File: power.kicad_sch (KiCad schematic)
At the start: 62 parts, among them J1 USB_C_Receptacle_USB2.0_14P, Q2 Q_NMOS_GDS, SW2 SW_SPDT, U12 AT24CS08-STUM, U2 BQ25895RTW, U4 LM1117DT-3.3, U5 MCP4017-xxxxLT, U6 TPS25751DREFR_C30169739, U7 LM3478MA

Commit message: resistor values
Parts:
- F1: Comment (none) -> resetable please
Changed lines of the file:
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@@
 			)
 		)
-		(property "Comment" ""
+		(property "Comment" "resetable please"
 			(at 54.61 30.48 90)
 			(hide yes)

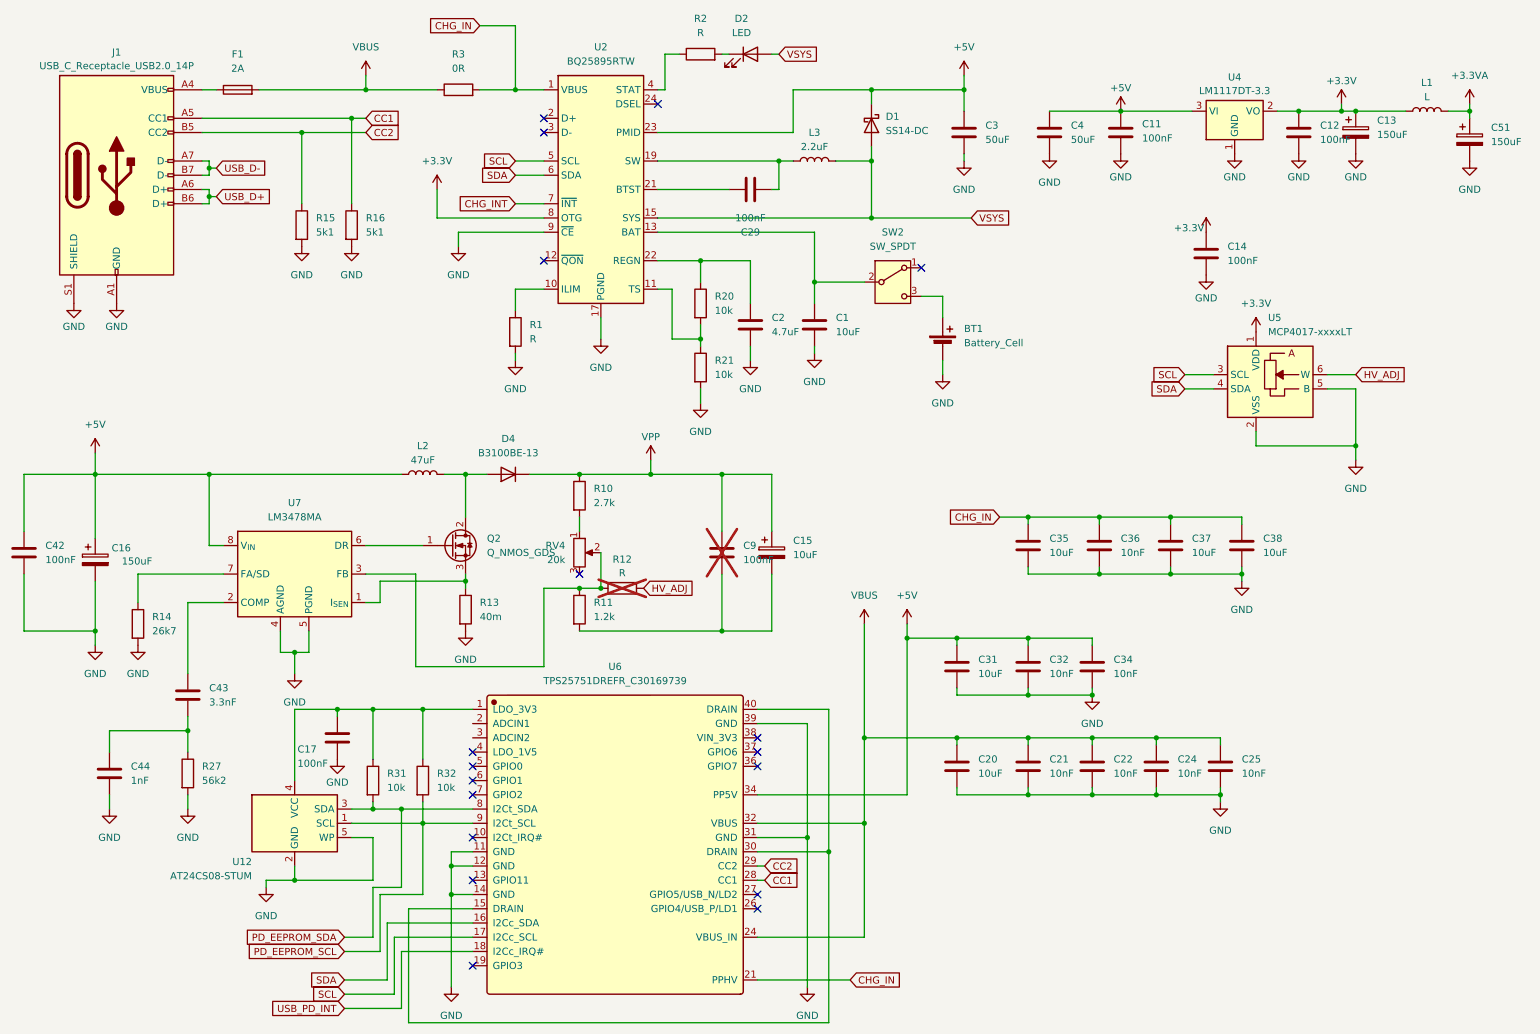
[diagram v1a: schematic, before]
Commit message: test points and small fix
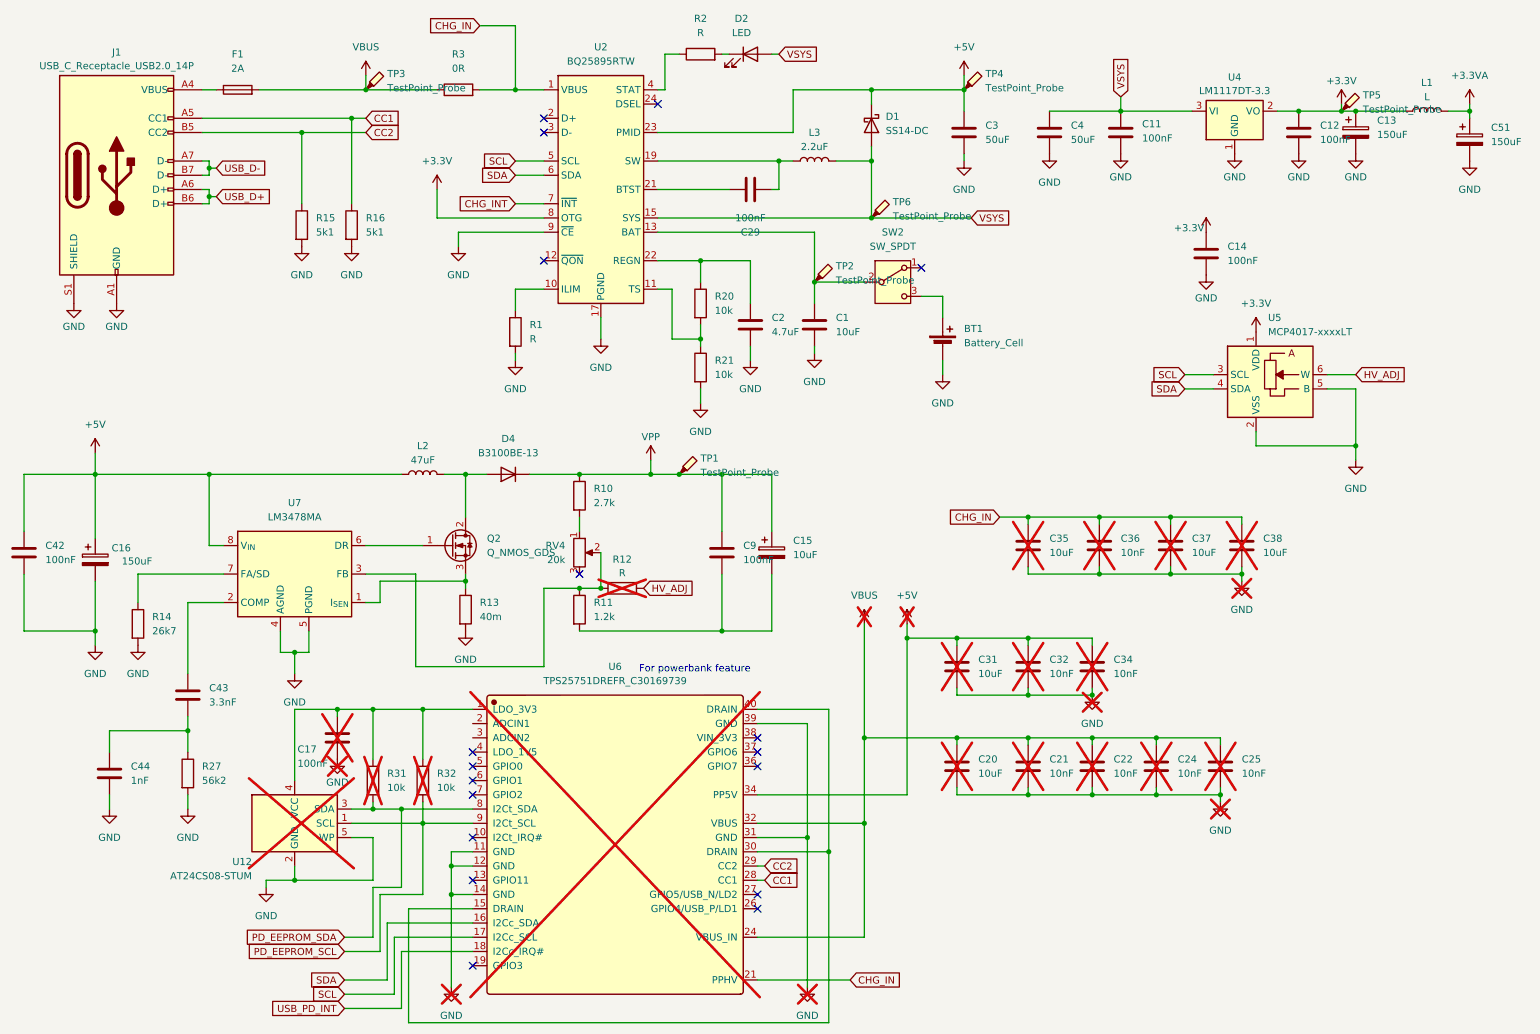
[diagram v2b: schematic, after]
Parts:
- added TP1, TP2, TP3, TP4, TP5, TP6: TestPoint_Probe, symbol Connector:TestPoint_Probe
- C17, C20, C21, C22, C24, C25, C31, C32, C34, C35, C36, C37, C38, R31, R32, U12, U6: now not fitted
- C9: now fitted
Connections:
- net +3.3V: now also TP5.1
- net +5V: now also TP4.1; no longer C11.1, C4.1, U4.3 (VI)
- net VBUS: now also TP3.1
- net VPP: now also TP1.1
- net VSYS: now also C11.1, C4.1, U4.3 (VI), TP6.1
- net at C1.1, SW2.2 (B), U2.13 (BAT)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: now also TP2.1
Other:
- note added: "For powerbank feature"

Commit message: sensor heat and some testpoints
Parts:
- TP1, TP2, TP3, TP4, TP5, TP6: footprint (none) -> TestPoint:TestPoint_THTPad_D2.0mm_Drill1.0mm
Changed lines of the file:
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@@
 			)
 		)
-		(property "Footprint" ""
+		(property "Footprint" "TestPoint:TestPoint_THTPad_D2.0mm_Drill1.0mm"
 			(at 172.72 53.34 0)
 			(hide yes)
@@
 			)
 		)
-		(property "Footprint" ""
+		(property "Footprint" "TestPoint:TestPoint_THTPad_D2.0mm_Drill1.0mm"
 			(at 82.55 30.48 0)
 			(hide yes)
@@
 			)
 		)
-		(property "Footprint" ""
+		(property "Footprint" "TestPoint:TestPoint_THTPad_D2.0mm_Drill1.0mm"
 			(at 162.56 64.77 0)
 			(hide yes)
@@
 			)
 		)
-		(property "Footprint" ""
+		(property "Footprint" "TestPoint:TestPoint_THTPad_D2.0mm_Drill1.0mm"
 			(at 189.23 30.48 0)
 			(hide yes)
@@
 			)
 		)
-		(property "Footprint" ""
+		(property "Footprint" "TestPoint:TestPoint_THTPad_D2.0mm_Drill1.0mm"
 			(at 256.54 34.29 0)
 			(hide yes)
@@
 			)
 		)
-		(property "Footprint" ""
+		(property "Footprint" "TestPoint:TestPoint_THTPad_D2.0mm_Drill1.0mm"
 			(at 138.43 99.06 0)
 			(hide yes)

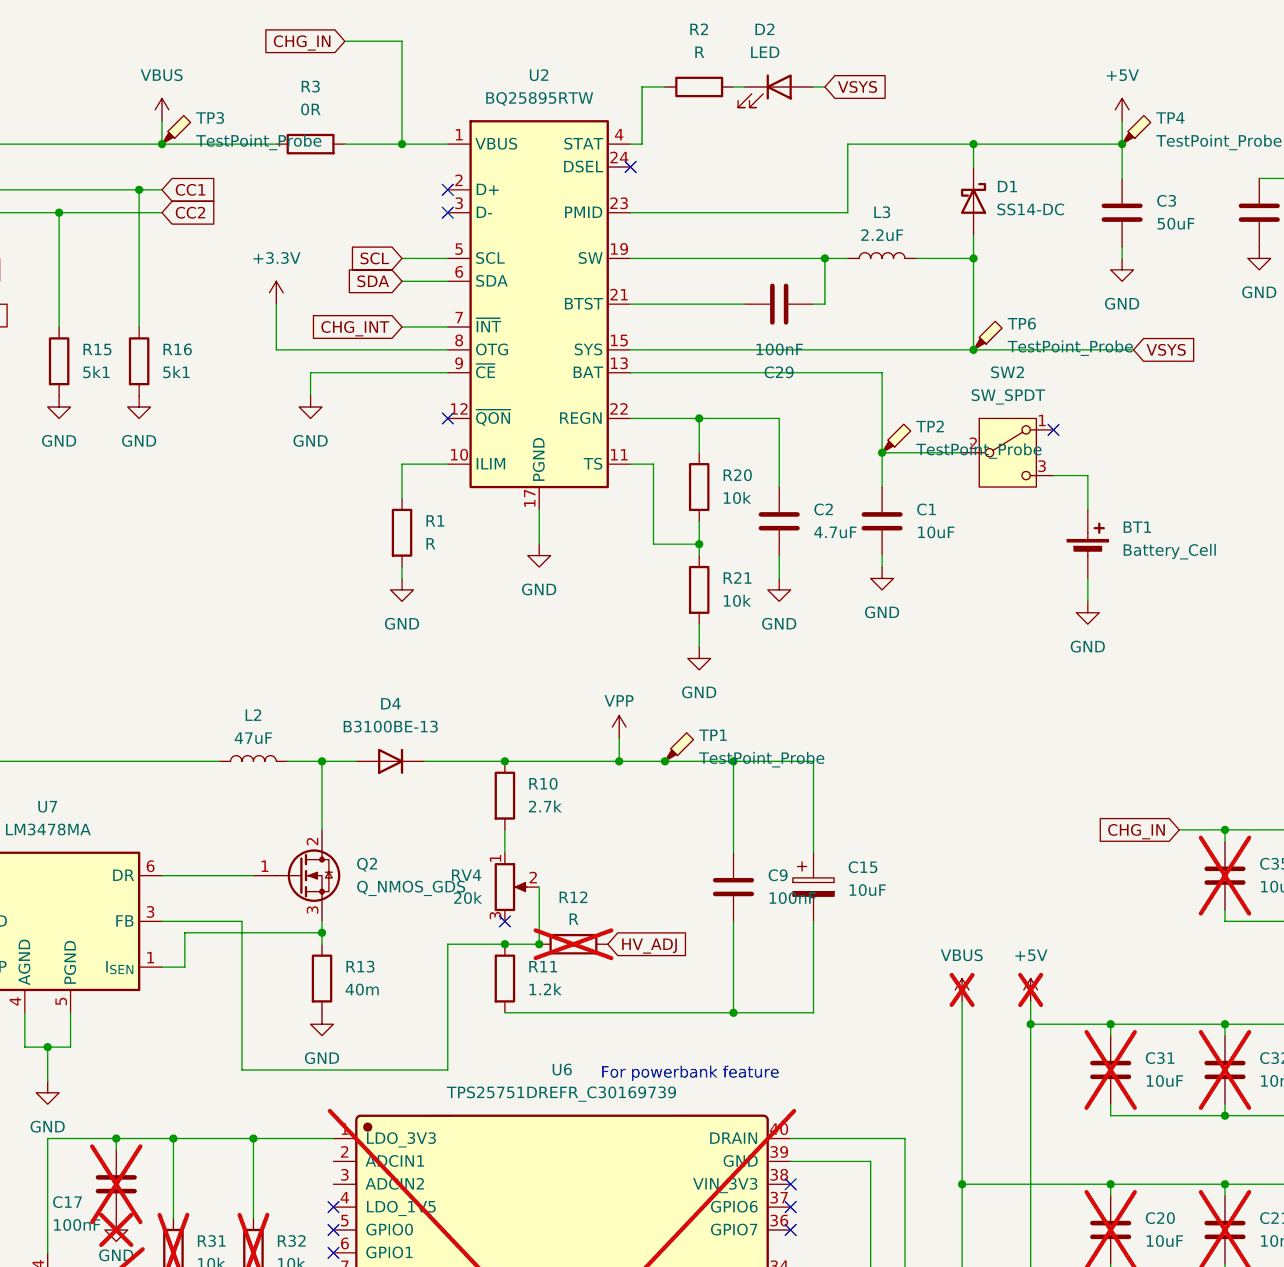
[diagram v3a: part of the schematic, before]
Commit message: some parts placement
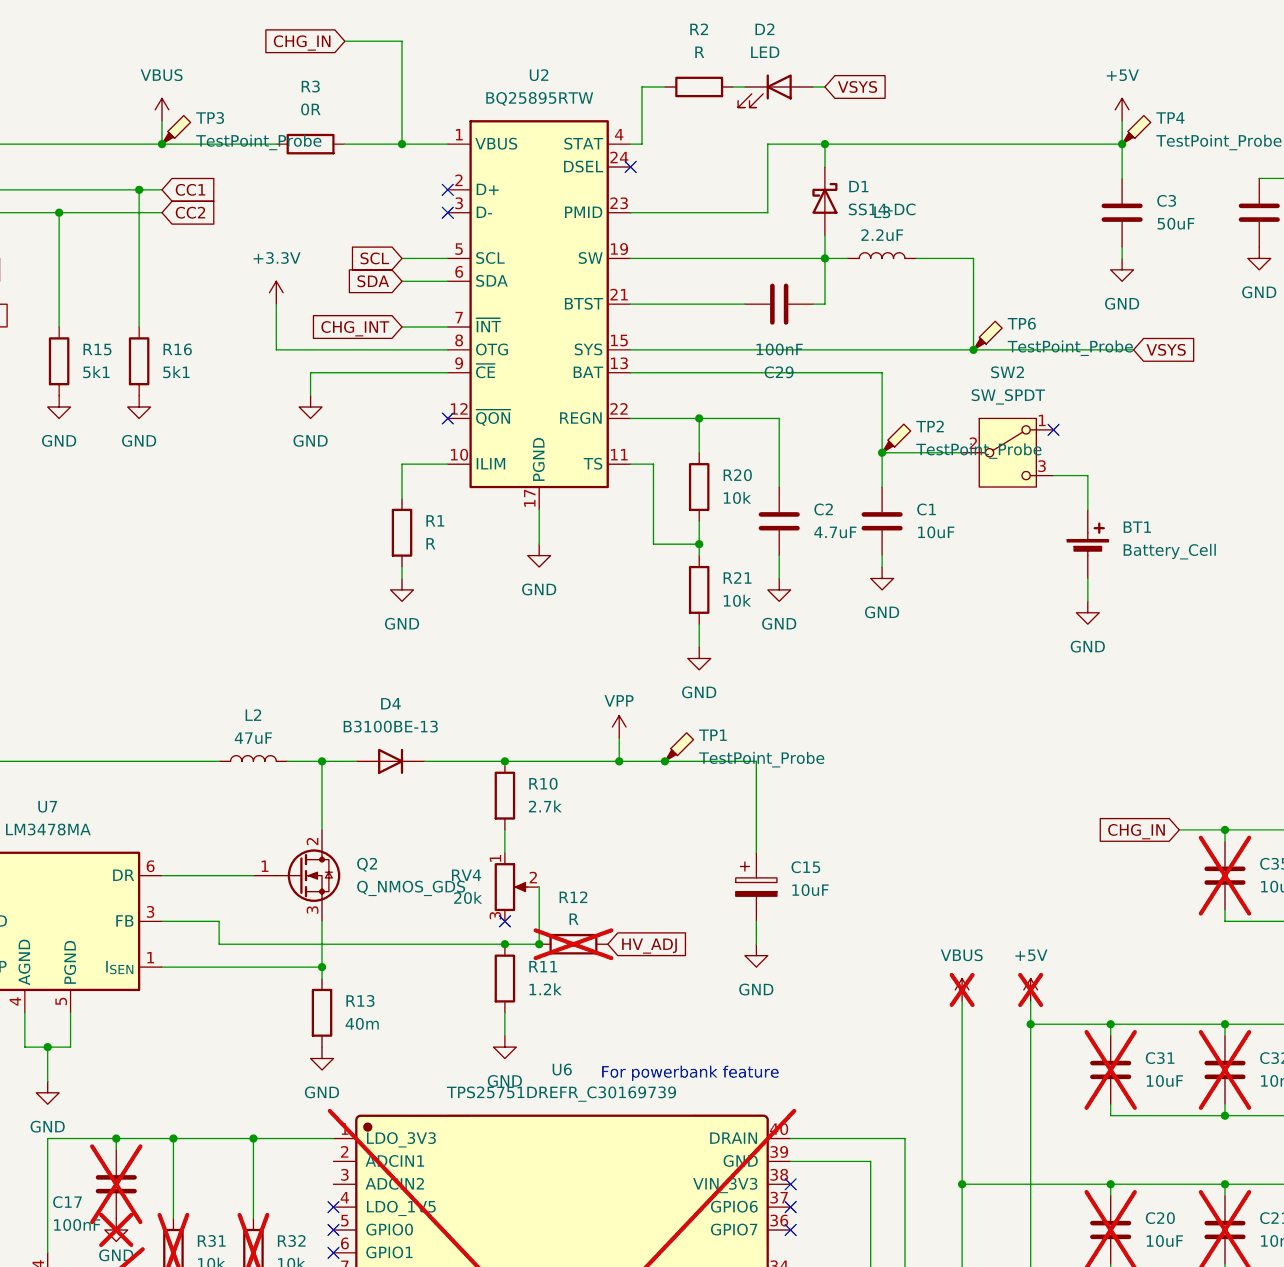
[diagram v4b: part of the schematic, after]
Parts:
- removed C9: 100nF, Capacitor_SMD:C_2220_5750Metric, symbol Device:C
- D1: footprint (none) -> Diode_SMD:D_SMA
- SW2: footprint Button_Switch_THT:SW_XKB_DM1-16UD-1 -> Button_Switch_SMD:SW_SPDT_CK_JS102011SAQN
- U12: footprint (none) -> Package_TO_SOT_SMD:SOT-23-5
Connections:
- net GND: now also C15.2, R11.2
- net VSYS: no longer D1.2 (A)
- net at C29.1, L3.1, U2.19 (SW)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: now also D1.2 (A)
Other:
- moved on the sheet: C15, R13

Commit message: Component changes, some new feature
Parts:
- removed C15: 10uF, Capacitor_SMD:CP_Elec_5x4.5, symbol Device:C_Polarized
- removed C16: 150uF, Capacitor_SMD:CP_Elec_5x4.5, symbol Device:C_Polarized
- removed C17: 100nF, Capacitor_SMD:C_0805_2012Metric, symbol Device:C
- removed C20, C31, C35, C37, C38: 10uF, Capacitor_SMD:C_0805_2012Metric, symbol Device:C
- removed C21, C22, C24, C25, C32, C34, C36: 10nF, Capacitor_SMD:C_0805_2012Metric, symbol Device:C
- removed R31, R32: 10k, Resistor_SMD:R_0805_2012Metric, symbol Device:R
- removed U12: AT24CS08-STUM, Package_TO_SOT_SMD:SOT-23-5, symbol Memory_EEPROM:AT24CS08-STUM
- removed U6: TPS25751DREFR_C30169739, JLCImport:TPS25751DREFR_C30169739, symbol JLCImport:TPS25751DREFR_C30169739
- added C16: 100uF, Capacitor_SMD:C_1206_3216Metric, symbol Device:C
- added C52: 10uF, Capacitor_SMD:C_1206_3216Metric, symbol Device:C
- added R6: 10k, Resistor_SMD:R_0805_2012Metric, symbol Device:R
- added U16: 74LVC1G125, Package_TO_SOT_SMD:Texas_R-PDSO-G5_DCK-5, symbol 74xGxx:74LVC1G125
- C13, C51: value 150uF -> 100uF; footprint Capacitor_SMD:CP_Elec_5x4.5 -> Capacitor_SMD:C_1206_3216Metric; symbol Device:C_Polarized -> Device:C; TME_SYMBOL EEEFT1A151AR -> CS3216X5R107M100NR
- C4: value 50uF -> 47uF; TME_SYMBOL (none) -> AMK212BC6476MG-T
- D1: value SS14-DC -> SBA120CS-R1; footprint Diode_SMD:D_SMA -> Diode_SMD:D_SOD-323; TME_SYMBOL (none) -> SBA120CS-R1
- D4: value B3100BE-13 -> SDB160WS-AQ-DIO; footprint Diode_SMD:D_SMB -> Diode_SMD:D_SOD-323; TME_SYMBOL B3100BE-13 -> SDB160WS-AQ-DIO
- L1: value L -> 100uH; footprint Inductor_SMD:L_1812_4532Metric -> Inductor_SMD:L_0805_2012Metric
- L2: value 47uF -> 100uH; Comment already have -> (none)
- L3: value 2.2uF -> 2.2uH; footprint Inductor_SMD:L_Bourns_SRP1038C_10.0x10.0mm -> Inductor_SMD:L_Taiyo-Yuden_NR-50xx; Comment already have -> (none); TME_SYMBOL PSDB1004NT101 -> DJNR5040-2R2-S; now in the parts list
- Q2: footprint Package_TO_SOT_SMD:TO-263-2 -> Package_TO_SOT_SMD:TO-252-3_TabPin2
- R10: value 2.7k -> 10k
- U4: footprint Package_TO_SOT_SMD:TO-252-3_TabPin2 -> Package_TO_SOT_SMD:SOT-223-3_TabPin2; symbol Regulator_Linear:LM1117DT-3.3 -> Regulator_Linear:LM1117MP-3.3
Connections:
- net +5V: now also C16.1, U16.2, U16.5 (VCC)
- net GND: now also C16.2, C52.2, R6.2, U16.3 (GND)
- net VPP: now also C52.1
- net at R14.1, U7.7 (FA/SD): now also U16.4
- new net HV_EN: R6.1, U16.1
- no-connect marks 18 -> 6
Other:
- note added: "1.26V"
- note added: "VPP=30V"
- note removed: "For powerbank feature"
- moved on the sheet: C42, C43, C44, D4, L2, Q2, R10, R11, R12, R13, R14, R27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

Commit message: Do compoent placing
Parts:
- removed BT1: Battery_Cell, Battery:BatteryHolder_MPD_BH-18650-PC, symbol Device:Battery_Cell
- added BT1, BT2: 247, 247:BAT_247, symbol 247:247
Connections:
- net GND: now also BT2.1_1, BT2.1_2, BT2.1_3
- net at SW2.3 (C): now also BT1.1_1, BT1.1_2, BT1.1_3
